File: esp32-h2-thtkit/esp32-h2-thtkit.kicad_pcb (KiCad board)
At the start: 4 copper layers, 17.9 x 21.9 mm, 25 parts, among them J1 PIN_GROUP_1, J2 PIN_GROUP_2, J3 UART, J6 PIN_GROUP_3, U2 ESP32-H2, U3 MIC5219-3.3YM5, Y1 32MHz ±10ppm CL8pF

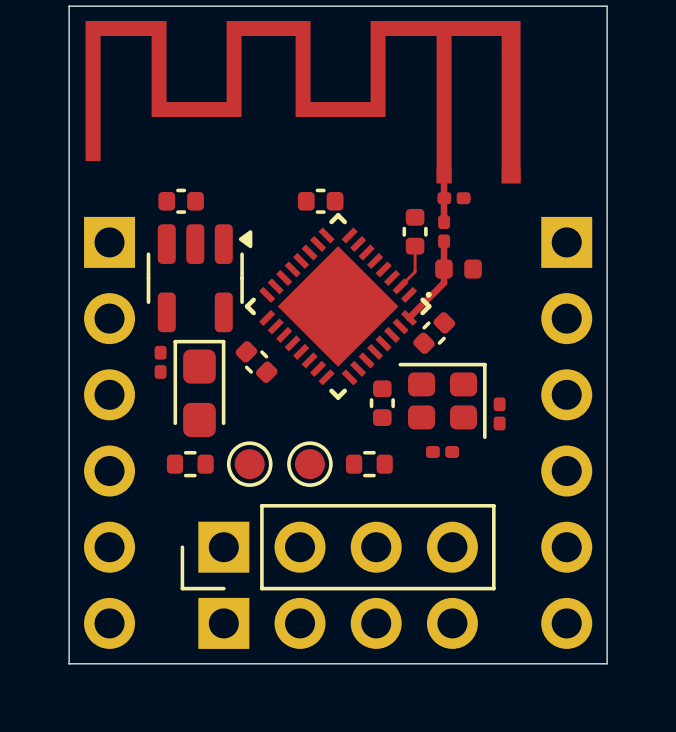
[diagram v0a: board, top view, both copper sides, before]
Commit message: Full schematic and PCB layout for esp32-h2 tht kit
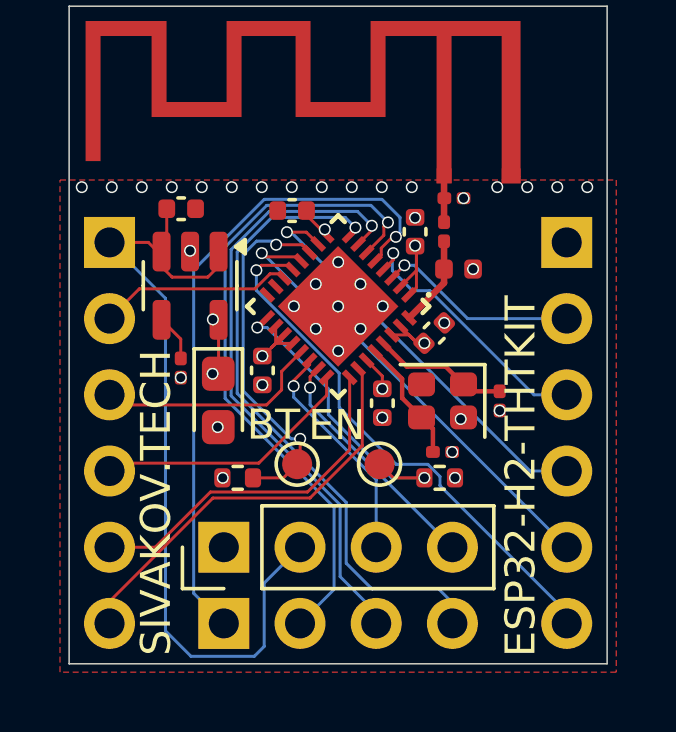
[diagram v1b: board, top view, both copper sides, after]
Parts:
- J1: value PIN_GROUP_1 -> PIN_GROUP_2
- J2: value PIN_GROUP_2 -> PIN_GROUP_1
- moved J1 15.2 mm to (145.4, 96.7)
- moved J2 15.2 mm to (130.2, 96.7)
- moved R2 2.39 mm to (141.2, 104.5)
- moved TP2 2.32 mm to (139.2, 104.1)
- moved R1 1.64 mm to (134.4, 104.5)
- moved TP1 1.58 mm to (136.4, 104.1)
- moved C5 1.00 mm to (136.3, 95.6)
- moved C13 0.70 mm to (132.6, 100.9)
- moved C15 0.67 mm to (133.8, 101.9)
- moved C8 0.43 mm to (143.2, 102.0)
- moved C7 0.34 mm to (135.3, 100.9), turned to 90 degrees
- moved U3 0.30 mm to (132.9, 98.1)
- moved C12 0.25 mm to (132.6, 95.5)
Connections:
- J1 pad 1: VIN -> GND
- J2 pad 1: GND -> VIN
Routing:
- net VIN: track 0.00 -> 28.3 mm
- net /MTMS: track 0.00 -> 22.6 mm, vias 0 -> 1
- net /MTDO: track 0.00 -> 22.1 mm, vias 0 -> 1
- net /MTDI: track 0.00 -> 21.6 mm, vias 0 -> 1
- net /MTCK: track 0.00 -> 20.7 mm, vias 0 -> 1
- net /GPIO11: track 0.00 -> 18.0 mm, vias 0 -> 1
- net /GPIO10: track 0.00 -> 16.3 mm, vias 0 -> 1
- net /GPIO8: track 0.00 -> 14.1 mm, vias 0 -> 1
- net /GPIO27: track 0.00 -> 13.9 mm
- net /BOOT: track 0.00 -> 12.4 mm, vias 0 -> 2
- net /GPIO26: track 0.00 -> 11.8 mm
- net +3.3V: track 1.54 -> 12.4 mm, vias 0 -> 9
- net /RESET: track 0.00 -> 10.3 mm, vias 0 -> 2
- net /GPIO25: track 0.00 -> 8.88 mm
- net /GPIO1: track 0.00 -> 8.80 mm, vias 0 -> 1
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- added copper zone on In2.Cu, net +3.3V
- added copper zone on F.Cu, net GND
- added copper zone on In1.Cu, net GND
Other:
- board text added: "BT"
- board text added: "EN"
- board text added: "ESP32-H2-THTKIT"
- board text added: "SIVAKOV.TECH"

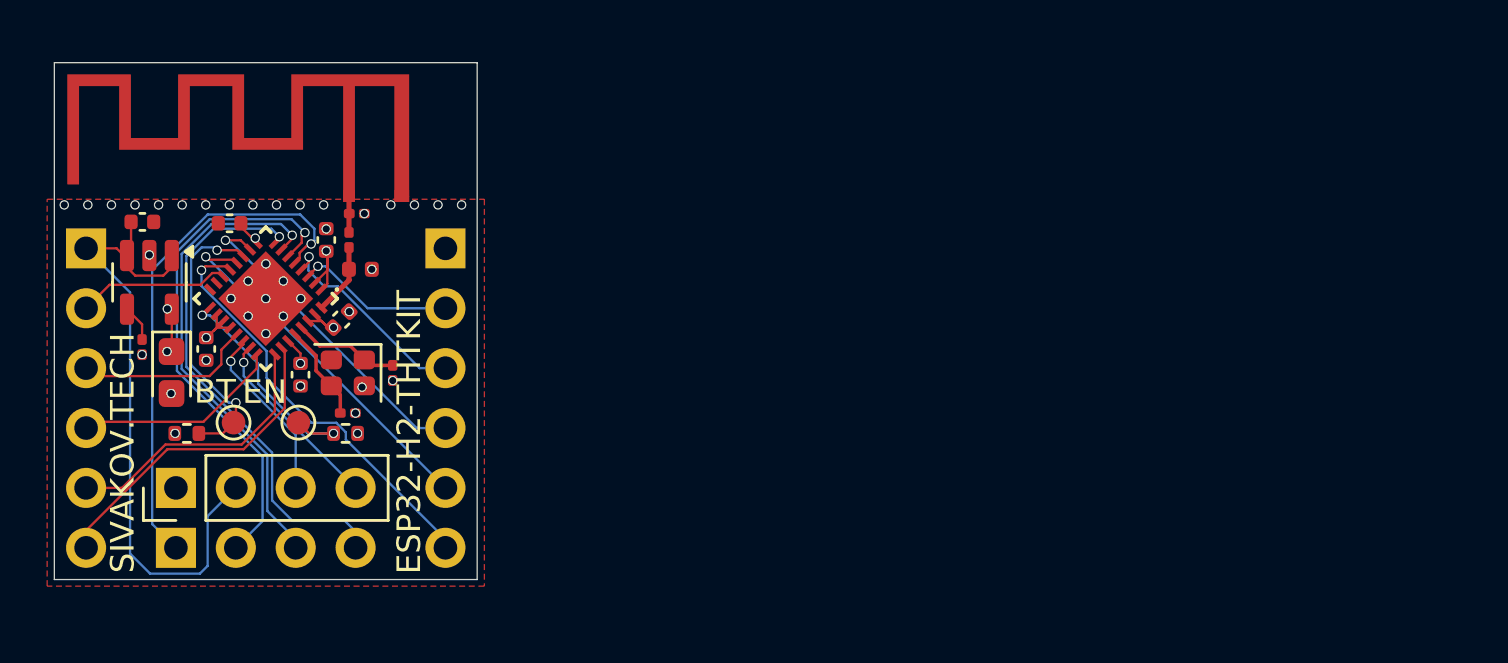
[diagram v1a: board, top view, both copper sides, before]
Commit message: Improve layout to make better SPI routes
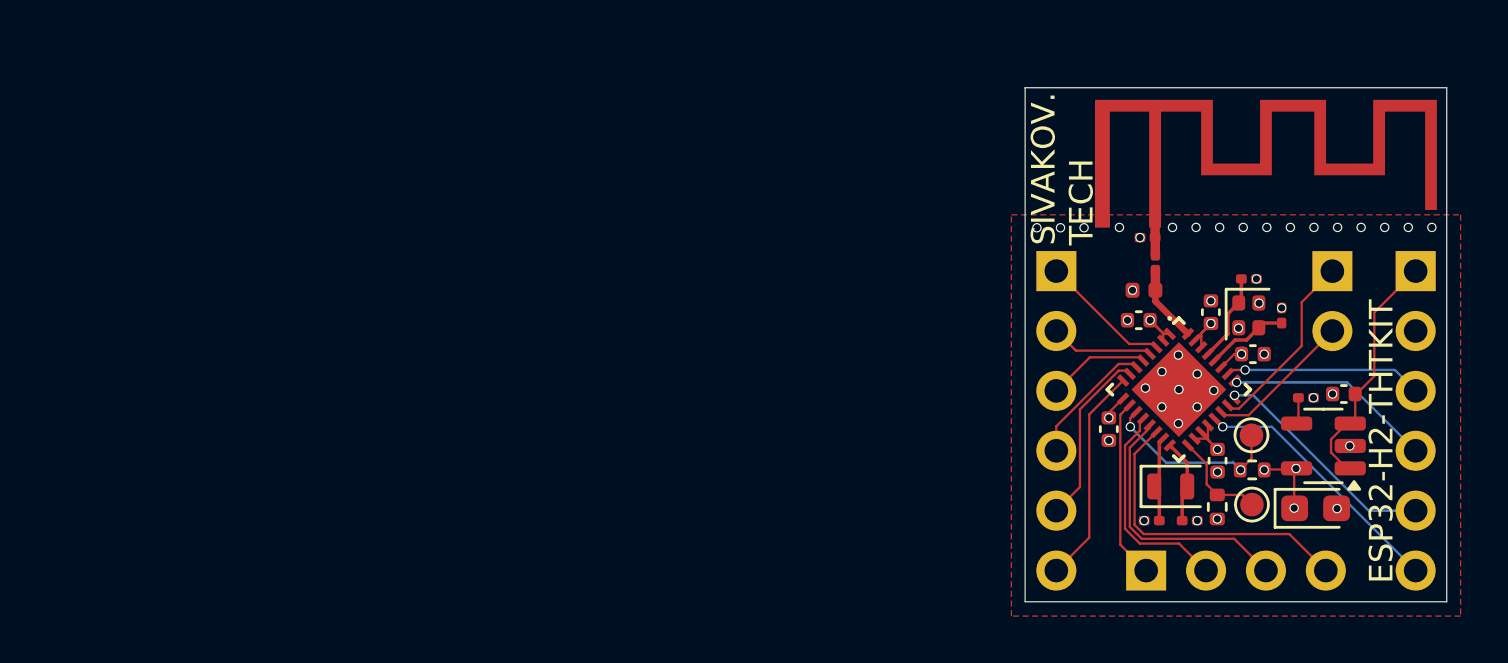
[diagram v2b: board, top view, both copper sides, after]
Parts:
- removed C15: 2.2m 6.3V TANT, Capacitor_Tantalum_SMD:CP_EIA-2012-12_Kemet-R
- removed J6: PIN_GROUP_3, PCM_SKC_Connector_PinHeader_2.54mm:PinHeader_1x04_P2.54mm_Vertical_NoSilk
- removed U3: MIC5219-3.3YM5, Package_TO_SOT_SMD:SOT-23-5
- added C1: 1m 6.3V X7R, Capacitor_SMD:C_0402_1005Metric, F.Cu at (183.5, 102.8)
- added C14: 6p 6.3V C0G, Capacitor_SMD:C_0201_0603Metric, F.Cu at (180.9, 99.5)
- added C2: 470p 6.3V X7R, Capacitor_SMD:C_0201_0603Metric, F.Cu at (181.9, 103.0)
- added J4: UART, PCM_SKC_Connector_PinHeader_2.54mm:PinHeader_1x02_P2.54mm_Vertical_NoSilk, F.Cu at (183.0, 97.6)
- added REF**: SIVAKOV_TECH_Circle_Medium_D13.22_1, SIVAKOV.TECH:SIVAKOV_TECH_Circle_Medium_D13.22_1, B.Cu at (178.9, 102.8)
- added U1: MIC5219-3.3YM5, Package_TO_SOT_SMD:SOT-23-5, F.Cu at (182.7, 105.1)
- added Y2: 32MHz ±10ppm CL8pF, PCM_SKC_Crystals:Crystal_SMD_1612-4Pin_1.6x1.2mm, F.Cu at (179.5, 99.5)
- AE1: footprint PCM_SKC_Antennas_SMD:Antenna_PCB_Espressif_2.4GHz_Left -> PCM_SKC_Antennas_SMD:Antenna_PCB_Espressif_2.4GHz_Right
- C11: value 8p 6.3V C0G -> 6p 6.3V C0G
- C12: value 1m 6.3V X7R -> 15p 6.3V C0G; footprint Capacitor_SMD:C_0402_1005Metric -> Capacitor_SMD:C_0201_0603Metric
- C13: value 470p 6.3V X7R -> 15p 6.3V C0G
- C3: value 100n 6.3V X7R -> 2.2m 6.3V TANT; footprint Capacitor_SMD:C_0402_1005Metric -> Capacitor_Tantalum_SMD:CP_EIA-2012-12_Kemet-R
- C4: value 5.6p C0G -> 100n 6.3V X7R; footprint Capacitor_SMD:C_0201_0603Metric -> Capacitor_SMD:C_0402_1005Metric
- C6: value 2.2p C0G -> 100n 6.3V X7R; footprint Capacitor_SMD:C_0201_0603Metric -> Capacitor_SMD:C_0402_1005Metric
- C7: value 100n 6.3V X7R -> 5.6p C0G; footprint Capacitor_SMD:C_0402_1005Metric -> Capacitor_SMD:C_0201_0603Metric
- C8: value 8p 6.3V C0G -> 2.2p C0G
- J1: value PIN_GROUP_2 -> PIN_GROUP_1; moved to F.Cu
- J2: value PIN_GROUP_1 -> PIN_GROUP_3; moved to F.Cu
- J3: value UART -> PIN_GROUP_2; footprint Connector_PinHeader_2.54mm:PinHeader_1x04_P2.54mm_Vertical -> PCM_SKC_Connector_PinHeader_2.54mm:PinHeader_1x04_P2.54mm_Vertical_NoSilk
- TP1, TP2: value TestPoint_2Pole -> TestPoint
- Y1: value 32MHz ±10ppm CL8pF -> 32.768kHz ±20ppm CL12.5pF; footprint Crystal:Crystal_SMD_2016-4Pin_2.0x1.6mm -> Crystal:Crystal_SMD_2012-2Pin_2.0x1.2mm
- moved J2 56.4 mm to (186.6, 97.6), turned to 0 degrees
- moved R1 45.2 mm to (179.6, 106.1), turned to 0 degrees
- moved C13 45.0 mm to (177.0, 108.2), turned to 180 degrees
- moved C12 44.6 mm to (175.4, 108.2), turned to 0 degrees
- moved AE1 43.6 mm to (180.2, 92.7)
- moved C3 43.5 mm to (182.3, 107.7), turned to 0 degrees
- moved TP1 43.2 mm to (179.6, 104.6), turned to 0 degrees
- moved J3 41.3 mm to (175.1, 110.3)
- moved TP2 40.6 mm to (179.6, 107.5), turned to 0 degrees
- moved C7 40.4 mm to (175.5, 97.3), turned to -90 degrees
- moved C9 40.4 mm to (179.7, 101.2), turned to 180 degrees
- moved U2 38.9 mm to (176.5, 102.7), turned to -45 degrees
- moved C11 38.6 mm to (179.5, 98.0), turned to 0 degrees
- moved C5 38.3 mm to (173.6, 104.3), turned to 90 degrees
- moved C6 38.0 mm to (178.2, 105.7), turned to 90 degrees
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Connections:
- C11 pad 1: GND -> /XTAL_P
- C11 pad 2: /XTAL_N -> GND
- C12 pad 2: VIN -> /XTAL_32K_P
- C13 pad 2: Net-(U3-BP) -> /XTAL_32K_N
- C3 pad 1: GND -> +3.3V
- C3 pad 2: +3.3V -> GND
- C4 pad 1: Net-(AE1-FEED) -> GND
- C4 pad 2: /RF -> +3.3V
- C6 pad 2: Net-(AE1-FEED) -> +3.3V
- C7 pad 1: GND -> Net-(AE1-FEED)
- C7 pad 2: +3.3V -> /RF
- C8 pad 1: /XTAL_P -> GND
- C8 pad 2: GND -> Net-(AE1-FEED)
- J1 pad 1: GND -> /GPIO0
- J1 pad 2: /GPIO0 -> /GPIO1
- J1 pad 3: /GPIO1 -> /MTMS
- J1 pad 4: /GPIO8 -> /MTDO
- J1 pad 5: /GPIO10 -> /MTCK
- J1 pad 6: /GPIO11 -> /MTDI
- J2 pad 2: /GPIO12 -> GND
- J2 pad 3: /GPIO22 -> /GPIO27
- J2 pad 4: /GPIO25 -> /GPIO26
- J2 pad 5: /GPIO26 -> /GPIO25
- J2 pad 6: /GPIO27 -> /GPIO22
- J3 pad 1: GND -> /GPIO8
- J3 pad 2: VIN -> /GPIO10
- J3 pad 3: /TX -> /GPIO11
- J3 pad 4: /RX -> /GPIO12
- U2 pad 15: unconnected-(U2-XTAL_32K_P-Pad15) -> /XTAL_32K_P
- U2 pad 16: unconnected-(U2-XTAL_32K_N-Pad16) -> /XTAL_32K_N
- U2 pad 22: /TX -> /U0RXD
- U2 pad 23: /RX -> /U0TXD
- Y1 pad 1: /XTAL_P -> /XTAL_32K_P
- Y1 pad 2: GND -> /XTAL_32K_N
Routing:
- net /MTMS: track 22.6 -> 4.33 mm, vias 1 -> 0
- net VIN: track 28.3 -> 11.1 mm
- net /MTDO: track 22.1 -> 5.59 mm, vias 1 -> 0
- net /MTCK: track 20.7 -> 7.56 mm, vias 1 -> 0
- net /MTDI: track 21.6 -> 9.23 mm, vias 1 -> 0
- net /RX: track 8.02 -> 0.00 mm, vias 1 -> 0
- net /U0TXD: track 0.00 -> 7.98 mm
- net /TX: track 7.59 -> 0.00 mm, vias 1 -> 0
- net /GPIO10: track 16.3 -> 9.16 mm, vias 1 -> 0
- net /GPIO11: track 18.0 -> 11.2 mm, vias 1 -> 0
- net /GPIO12: track 6.50 -> 13.2 mm
- net /GPIO8: track 14.1 -> 7.63 mm, vias 1 -> 0
- net /U0RXD: track 0.00 -> 6.25 mm
- net /RESET: track 10.3 -> 4.26 mm, vias 2 -> 0
- net /GPIO27: track 13.9 -> 8.40 mm, vias 0 -> 1
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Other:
- board size 17.9 x 21.9 mm -> 17.9 x 21.8 mm
- board text added: "SIVAKOV. TECH"
- board text removed: "BT"
- board text removed: "EN"
- board text removed: "SIVAKOV.TECH"

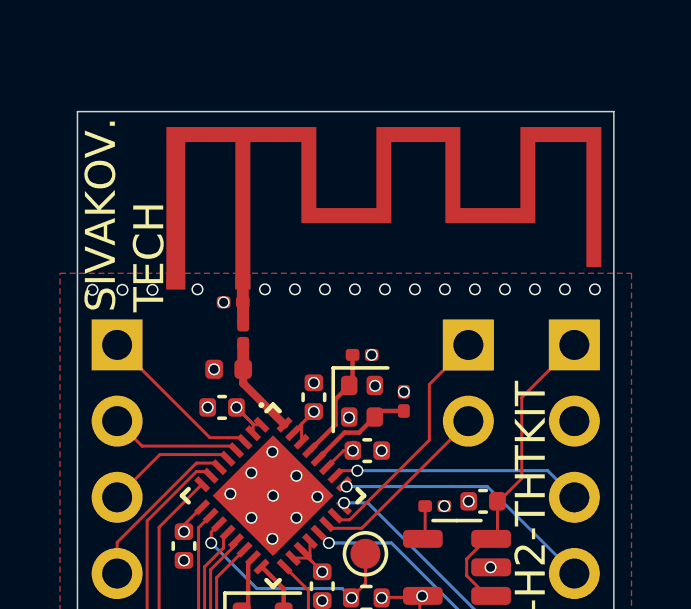
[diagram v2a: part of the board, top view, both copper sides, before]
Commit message: Fix antenna layout a bit
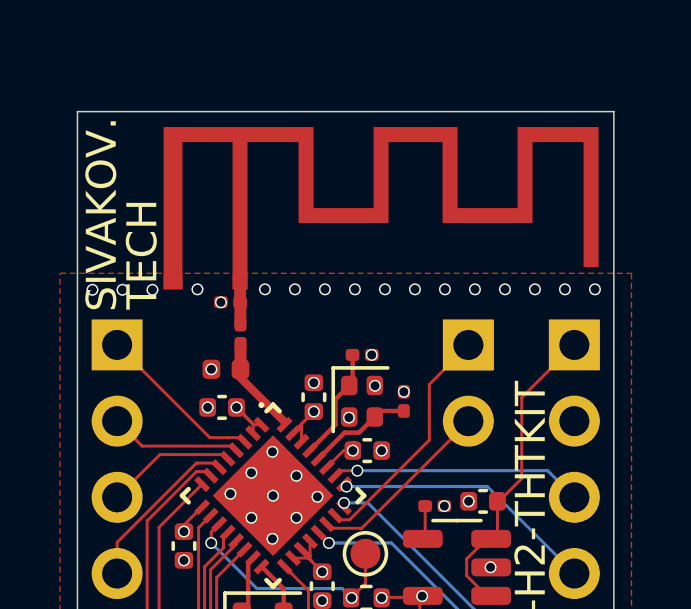
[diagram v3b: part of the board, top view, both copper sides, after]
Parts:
- moved AE1 0.09 mm to (180.1, 92.7)
- moved C7 0.09 mm to (175.4, 97.3)
- moved C8 0.09 mm to (175.1, 96.2)
- moved L1 0.09 mm to (174.9, 98.5)
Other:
- board text added: "SIVAKOV."
- board text added: "TECH"
- board text removed: "SIVAKOV. TECH"
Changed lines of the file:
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@@
 	(footprint "Inductor_SMD:L_0402_1005Metric"
 		(layer "F.Cu")
-		(at 175.04 98.45 180)
+		(at 174.95 98.45 180)
 		(descr "Inductor SMD 0402 (1005 Metric), square (rectangular) end terminal, IPC-7351 nominal, (Body size source: http://www.tortai-tech.com/upload/download/2011102023233369053.pdf), generated with kicad-footprint-generator")
 		(tags "inductor")
@@
 	(footprint "Capacitor_SMD:C_0201_0603Metric"
 		(layer "F.Cu")
-		(at 175.525 97.2816 -90)
+		(at 175.435 97.2816 -90)
 		(descr "Capacitor SMD 0201 (0603 Metric), square (rectangular) end terminal, IPC-7351 nominal, (Body size source: https://www.vishay.com/docs/20052/crcw0201e3.pdf), generated with kicad-footprint-generator")
 		(tags "capacitor")
@@
 	(footprint "Capacitor_SMD:C_0201_0603Metric"
 		(layer "F.Cu")
-		(at 175.1924 96.217)
+		(at 175.1024 96.217)
 		(descr "Capacitor SMD 0201 (0603 Metric), square (rectangular) end terminal, IPC-7351 nominal, (Body size source: https://www.vishay.com/docs/20052/crcw0201e3.pdf), generated with kicad-footprint-generator")
 		(tags "capacitor")
@@
 	(footprint "PCM_SKC_Antennas_SMD:Antenna_PCB_Espressif_2.4GHz_Right"
 		(layer "F.Cu")
-		(at 180.213 92.675)
+		(at 180.12 92.675)
 		(descr "PCB trace antenna for 2.4 GHz, as used on Espressif DevKitC and ESP32-MINI modules, right direction")
 		(tags "antenna pcb 2.4GHz esp32 esp8266 wroom wrover devkit esp-mc right")
@@
 			(polygon
 				(pts
-					(xy 187.893 89.995) (xy 187.893 95.355) (xy 172.533 95.355) (xy 172.533 89.995)
+					(xy 187.8 89.995) (xy 187.8 95.355) (xy 172.44 95.355) (xy 172.44 89.995)
 				)
 			)
@@
 		(layer "Edge.Cuts")
 	)
-	(gr_text "ESP32-H2-THTKIT"
-		(at 185.7 110.89 90)
+	(gr_text "TECH"
+		(at 172.75 96.46 90)
 		(layer "F.SilkS")
 		(effects
@@
 		)
 	)
-	(gr_text "SIVAKOV.\nTECH"
-		(at 172.98 96.55 90)
+	(gr_text "SIVAKOV."
+		(at 171.4 96.54 90)
+		(layer "F.SilkS")
+		(effects
+			(font
+				(size 1 1)
+				(thickness 0.15)
+			)
+			(justify left bottom)
+		)
+	)
+	(gr_text "ESP32-H2-THTKIT"
+		(at 185.7 110.89 90)
 		(layer "F.SilkS")
 		(effects
@@
 	)
 	(segment
-		(start 175.525 97.6114)
-		(end 175.5152 97.6016)
-		(width 0.1)
+		(start 176.90403 100.20403)
+		(end 175.31 98.61)
+		(width 0.27)
 		(layer "F.Cu")
 		(net 1)
 	)
 	(segment
-		(start 175.525 98.45)
-		(end 175.525 97.6114)
-		(width 0.4)
+		(start 176.90403 100.29887)
+		(end 176.90403 100.20403)
+		(width 0.1)
 		(layer "F.Cu")
 		(net 1)
 	)
 	(segment
-		(start 175.525 98.91984)
-		(end 176.90403 100.29887)
-		(width 0.27)
+		(start 175.525 97.6114)
+		(end 175.5152 97.6016)
+		(width 0.1)
 		(layer "F.Cu")
 		(net 1)
 	)
 	(segment
-		(start 175.525 98.45)
-		(end 175.525 98.91984)
-		(width 0.27)
+		(start 175.435 98.45)
+		(end 175.435 97.6114)
+		(width 0.4)
 		(layer "F.Cu")
 		(net 1)
@@
 	)
 	(via
-		(at 174.555 98.45)
+		(at 174.465 98.45)
 		(size 0.4)
 		(drill 0.3)
@@
 	)
 	(via
-		(at 174.8724 96.217)
+		(at 174.7824 96.217)
 		(size 0.4)
 		(drill 0.3)
@@
 	)
 	(segment
-		(start 175.5124 96.217)
-		(end 175.5124 95.5356)
+		(start 175.4224 96.217)
+		(end 175.4224 95.5356)
 		(width 0.4)
 		(layer "F.Cu")
@@
 	)
 	(segment
-		(start 175.52 96.9616)
-		(end 175.52 96.2246)
+		(start 175.43 96.9616)
+		(end 175.43 96.2246)
 		(width 0.4)
 		(layer "F.Cu")

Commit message: Draw pin layout on user layer
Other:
- board text added: "BOOT"
- board text added: "GND"
- board text added: "GPIO0"
- board text added: "GPIO1"
- board text added: "GPIO10"
- board text added: "GPIO11"
- board text added: "GPIO12"
- board text added: "GPIO22"
- board text added: "GPIO25"
- board text added: "GPIO26"
- board text added: "GPIO27"
- board text added: "GPIO8"
- board text added: "MTCK"
- board text added: "MTDI"
- board text added: "MTDO"
- board text added: "MTMS"
- board text added: "RESET"
- board text added: "RX"
- board text added: "TX"
- board text added: "VIN"

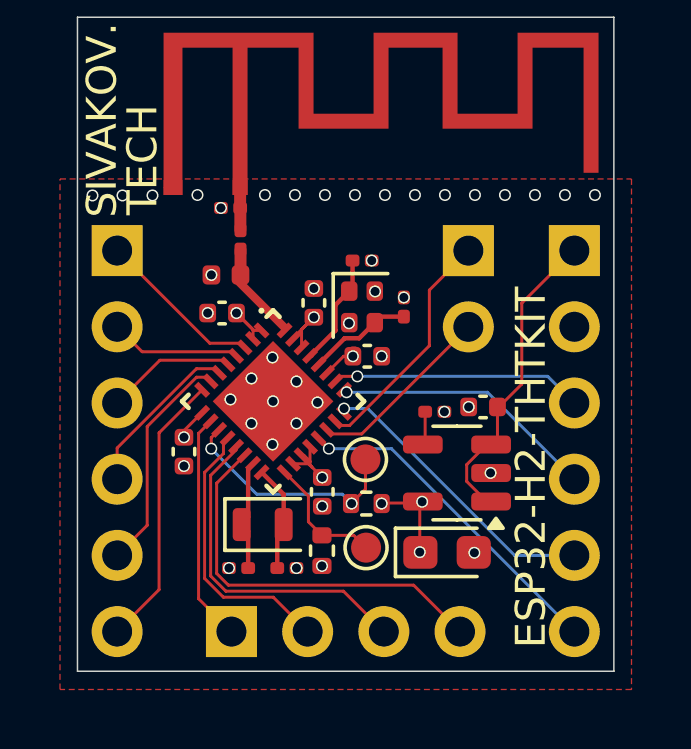
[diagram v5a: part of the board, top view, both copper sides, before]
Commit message: Make devkits cheaper by using 0402 components instead of 0201
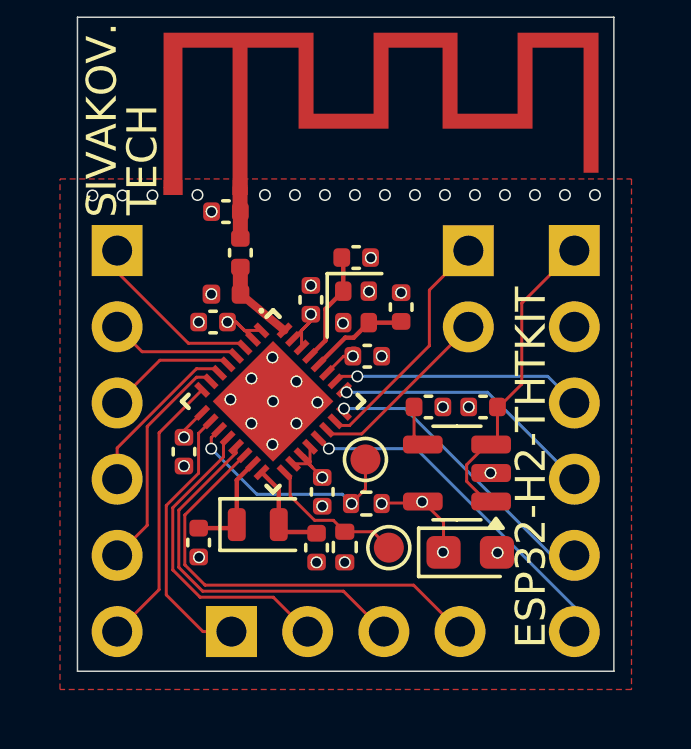
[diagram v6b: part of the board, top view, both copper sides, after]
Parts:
- C11, C14: value 6p 6.3V C0G -> 15p 6.3V C0G; footprint Capacitor_SMD:C_0201_0603Metric -> Capacitor_SMD:C_0402_1005Metric
- C12, C13: value 15p 6.3V C0G -> 25p 6.3V C0G; footprint Capacitor_SMD:C_0201_0603Metric -> Capacitor_SMD:C_0402_1005Metric
- C2, C7, C8: footprint Capacitor_SMD:C_0201_0603Metric -> Capacitor_SMD:C_0402_1005Metric
- moved C12 1.58 mm to (174.0, 107.4), turned to 90 degrees
- moved C13 1.20 mm to (178.0, 107.5), turned to 90 degrees
- moved C3 0.77 mm to (183.1, 107.7)
- moved R2 0.77 mm to (178.9, 107.5)
- moved TP2 0.76 mm to (180.4, 107.5)
- moved L1 0.64 mm to (174.9, 99.1)
- moved C7 0.43 mm to (175.4, 97.7)
- moved C4 0.42 mm to (174.5, 100.0)
- moved C2 0.26 mm to (181.7, 102.8)
- moved C11 0.22 mm to (179.3, 97.9)
- moved Y2 0.20 mm to (179.3, 99.5)
- moved C8 0.20 mm to (174.9, 96.3)
- moved Y1 0.16 mm to (176.0, 106.8)
- moved C10 0.14 mm to (177.8, 99.3)
- moved C14 0.09 mm to (180.8, 99.5)
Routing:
- net /RF: track 3.20 -> 0.90 mm
- net /GPIO8: track 7.63 -> 9.08 mm
- net /GPIO10: track 9.16 -> 10.5 mm
- net /GPIO11: track 11.2 -> 12.5 mm
- net /GPIO12: track 13.2 -> 14.6 mm
- net /RESET: track 4.26 -> 4.87 mm
- net +3.3V: track 13.4 -> 12.8 mm
